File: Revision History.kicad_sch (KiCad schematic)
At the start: 0 parts

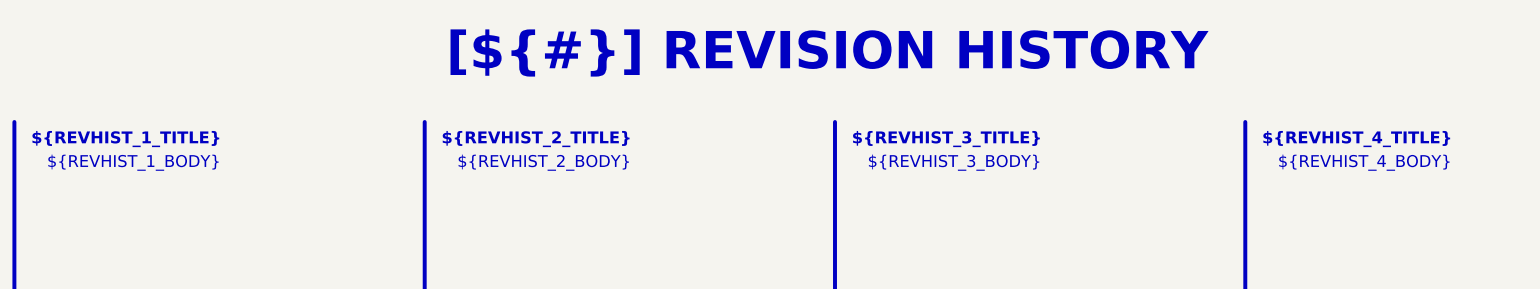
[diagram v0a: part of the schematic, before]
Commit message: test: exercise boardwright preview path
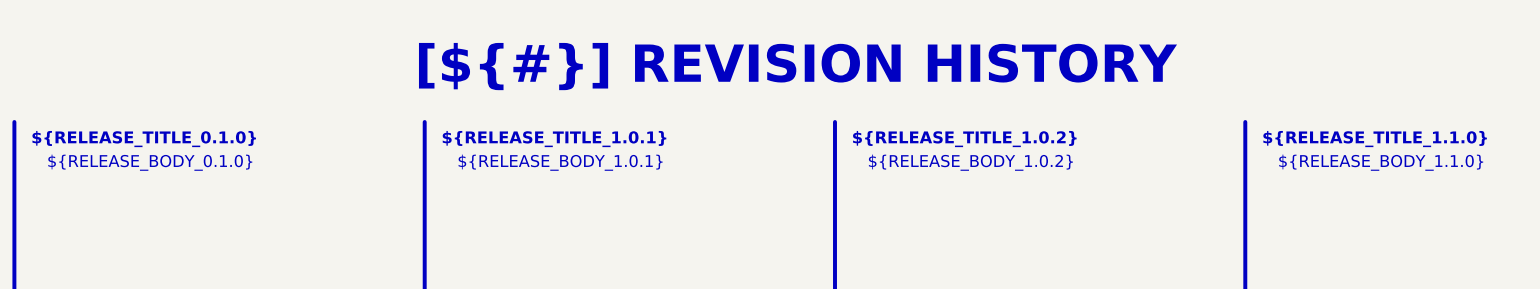
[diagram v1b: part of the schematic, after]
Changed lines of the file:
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@@
 	(title_block
 		(title "REVISION HISTORY")
-		(date "2025-01-12")
+		(date "2026-04-24")
 		(rev "${REVISION}")
 		(company "${COMPANY}")
 	)
-	(text_box "${REVHIST_4_BODY}"
+	(text_box "${RELEASE_BODY_1.1.0}"
 		(exclude_from_sim no)
 		(at 224.79 35.56 0)
@@
 		(stroke
 			(width -0.0001)
-			(type solid)
+			(type default)
 		)
 		(fill
@@
 	(text_box "[${#}] ${TITLE}"
 		(exclude_from_sim no)
-		(at 20.32 10.16 0)
-		(size 266.7 20.32)
+		(at 80.01 15 0)
+		(size 137.16 15)
 		(margins 4.4999 4.4999 4.4999 4.4999)
 		(stroke
@@
 		)
 	)
-	(text_box "${REVHIST_1_BODY}"
+	(text_box "${RELEASE_BODY_0.1.0}"
 		(exclude_from_sim no)
 		(at 26.67 35.56 0)
@@
 		)
 	)
-	(text_box "${REVHIST_3_TITLE}"
+	(text_box "${RELEASE_TITLE_1.0.2}"
 		(exclude_from_sim no)
 		(at 156.21 31.75 0)
@@
 		(stroke
 			(width -0.0001)
-			(type solid)
+			(type default)
 		)
 		(fill
@@
 		)
 	)
-	(text_box "${REVHIST_3_BODY}"
+	(text_box "${RELEASE_BODY_1.0.2}"
 		(exclude_from_sim no)
 		(at 158.75 35.56 0)
@@
 		(stroke
 			(width -0.0001)
-			(type solid)
+			(type default)
 		)
 		(fill
@@
 		)
 	)
-	(text_box "${REVHIST_2_BODY}"
+	(text_box "${RELEASE_BODY_1.0.1}"
 		(exclude_from_sim no)
 		(at 92.71 35.56 0)
@@
 		(stroke
 			(width -0.0001)
-			(type solid)
+			(type default)
 		)
 		(fill
@@
 		)
 	)
-	(text_box "${REVHIST_1_TITLE}"
+	(text_box "${RELEASE_TITLE_0.1.0}"
 		(exclude_from_sim no)
 		(at 24.13 31.75 0)
@@
 		)
 	)
-	(text_box "${REVHIST_2_TITLE}"
+	(text_box "${RELEASE_TITLE_1.0.1}"
 		(exclude_from_sim no)
 		(at 90.17 31.75 0)
@@
 		(stroke
 			(width -0.0001)
-			(type solid)
+			(type default)
 		)
 		(fill
@@
 		)
 	)
-	(text_box "${REVHIST_4_TITLE}"
+	(text_box "${RELEASE_TITLE_1.1.0}"
 		(exclude_from_sim no)
 		(at 222.25 31.75 0)
@@
 		(stroke
 			(width -0.0001)
-			(type solid)
+			(type default)
 		)
 		(fill
